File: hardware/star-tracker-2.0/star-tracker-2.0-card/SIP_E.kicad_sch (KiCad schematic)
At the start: 1 part, among them U7 OSD3358-512M-BSM

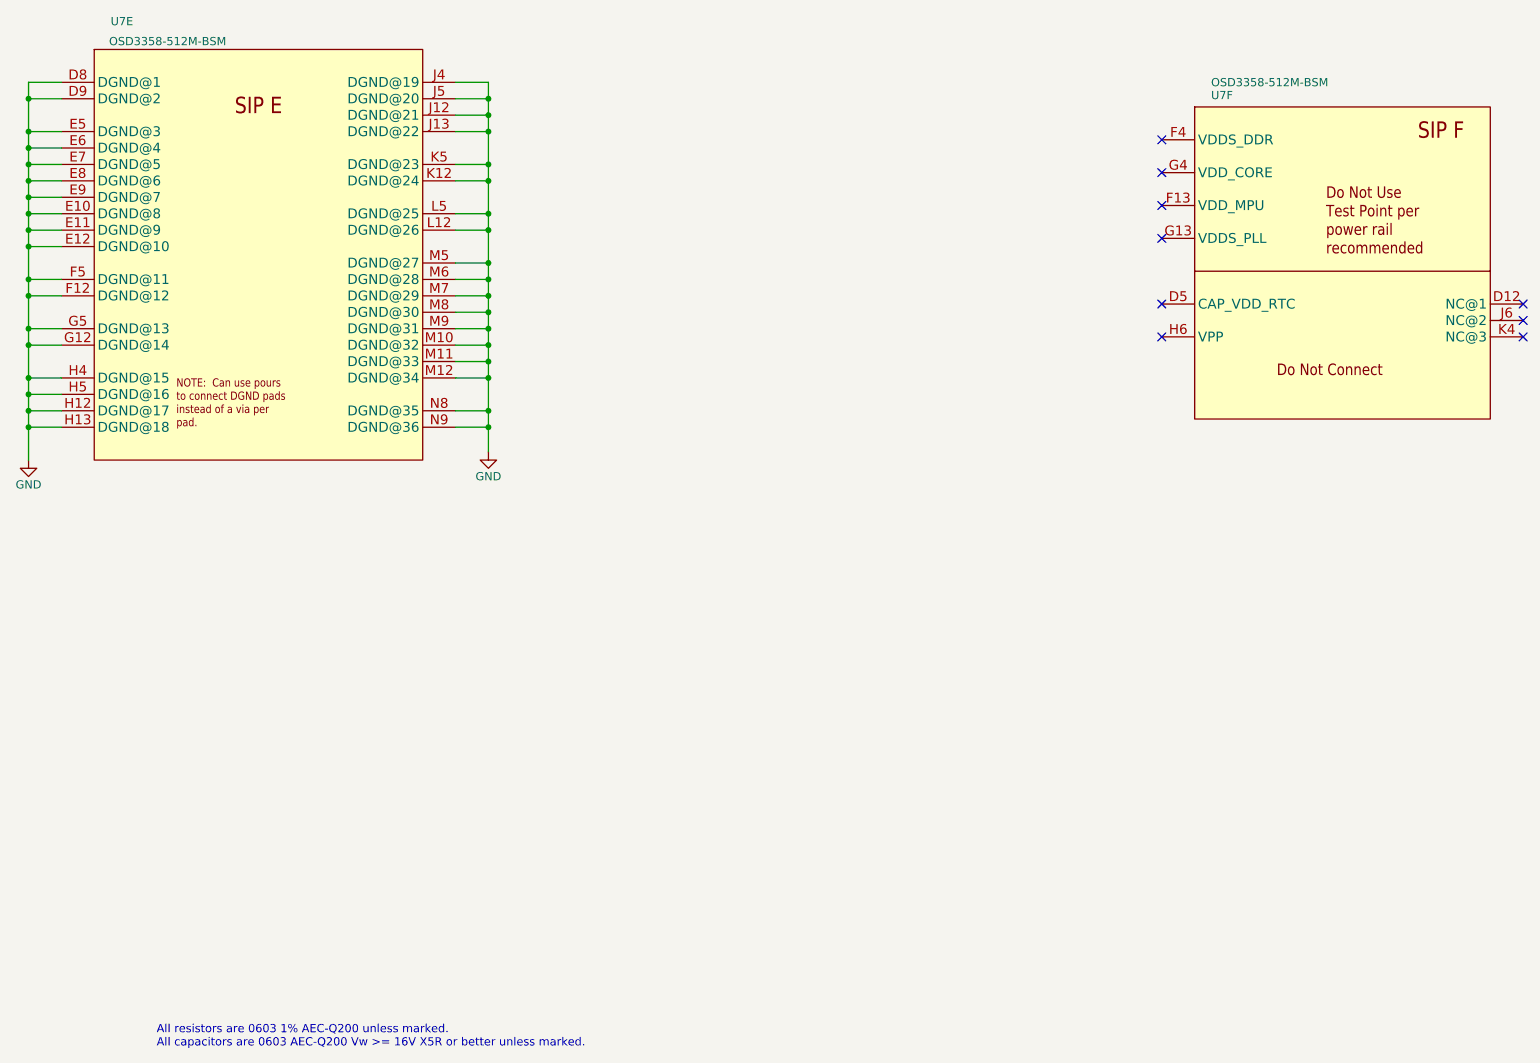
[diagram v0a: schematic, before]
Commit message: Star tracker board update
Added 3d models to footprints, reannotated component designators
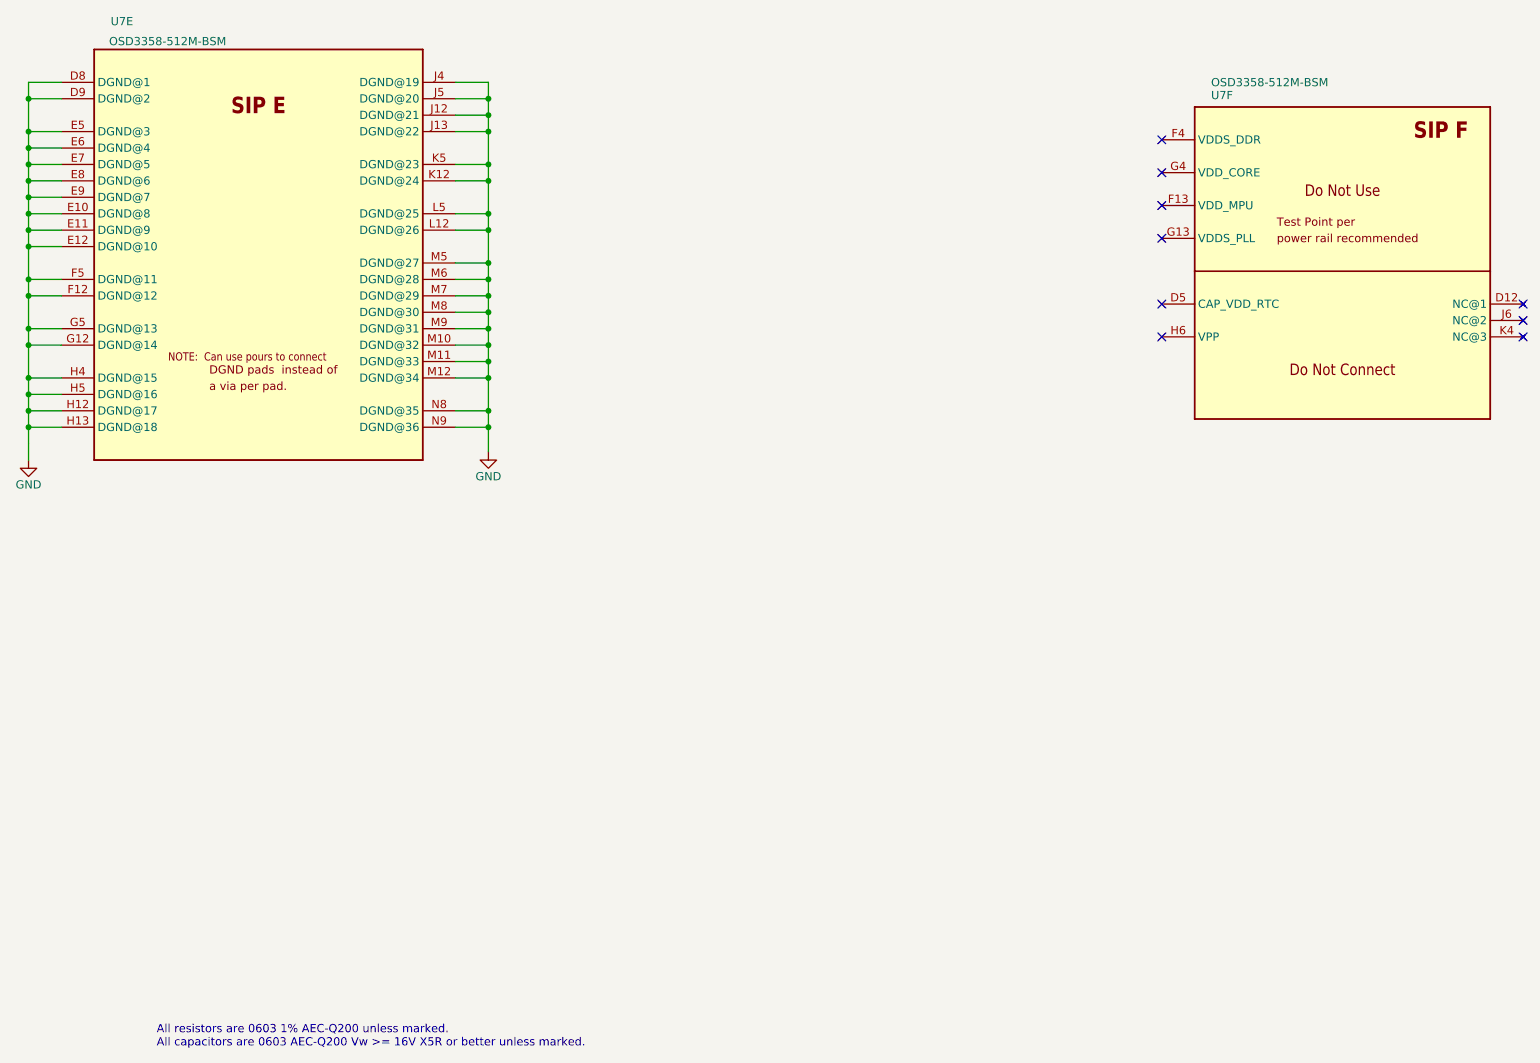
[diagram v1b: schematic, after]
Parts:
- U7: footprint star-tracker-card:OSD335X-BGA-256 -> oresat-ics:U-Octavo-OSD335X-BGA-256; symbol star-tracker-card-eagle-import:OSD3358-512M-BSM -> oresat-ics:OSD3358-512M-BSM; Distributor (none) -> DigiKey; MPN OSD3358-1G-ISM -> OSD3358-512M-BSM
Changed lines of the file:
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@@
 	(title_block
 		(title "OreSat Star Tracker")
-		(date "2026-04-22")
-		(rev "1.3")
+		(date "2026-06-05")
+		(rev "2.0")
 		(company "Portland State Aerospace Society")
 	)
@@
 	)
 	(symbol
-		(lib_id "star-tracker-card-eagle-import:OSD3358-512M-BSM")
+		(lib_id "oresat-ics:OSD3358-512M-BSM")
 		(at 128.27 142.24 0)
 		(unit 5)
@@
 			)
 		)
-		(property "Footprint" "star-tracker-card:OSD335X-BGA-256"
-			(at 128.27 142.24 0)
+		(property "Footprint" "oresat-ics:U-Octavo-OSD335X-BGA-256"
+			(at 128.27 34.29 0)
 			(hide yes)
 			(show_name no)
@@
 			)
 		)
-		(property "Description" "OSD335x Embedded Module ARM® Cortex®-A8, AM3358 1GHz 1GB"
-			(at 128.27 142.24 0)
+		(property "Description" "OSD335x Embedded Module 1GHz 512MB"
+			(at 128.27 38.1 0)
 			(hide yes)
 			(show_name no)
@@
 			)
 		)
-		(property "MPN" "OSD3358-1G-ISM"
-			(at 128.27 142.24 0)
+		(property "MPN" "OSD3358-512M-BSM"
+			(at 128.27 43.18 0)
+			(hide yes)
+			(show_name no)
+			(do_not_autoplace no)
+			(effects
+				(font
+					(size 1.27 1.27)
+				)
+			)
+		)
+		(property "Distributor" "DigiKey"
+			(at 128.27 40.64 0)
 			(hide yes)
 			(show_name no)
@@
 		(in_pos_files yes)
 		(dnp no)
-		(property "Reference" "#PWR74"
+		(property "Reference" "#PWR063"
 			(at 163.83 180.34 0)
 			(hide yes)
@@
 			(project "star-tracker-card"
 				(path "/324e9eb5-7420-4b7e-862c-cc20bb28618a/eb575624-9a53-42ad-b889-70334a877908"
-					(reference "#PWR74")
+					(reference "#PWR063")
 					(unit 1)
 				)
@@
 	)
 	(symbol
-		(lib_id "star-tracker-card-eagle-import:OSD3358-512M-BSM")
+		(lib_id "oresat-ics:OSD3358-512M-BSM")
 		(at 295.91 146.05 0)
 		(unit 6)
@@
 			)
 		)
-		(property "Footprint" "star-tracker-card:OSD335X-BGA-256"
-			(at 295.91 146.05 0)
+		(property "Footprint" "oresat-ics:U-Octavo-OSD335X-BGA-256"
+			(at 295.91 38.1 0)
 			(hide yes)
 			(show_name no)
@@
 			)
 		)
-		(property "Description" "OSD335x Embedded Module ARM® Cortex®-A8, AM3358 1GHz 1GB"
-			(at 295.91 146.05 0)
+		(property "Description" "OSD335x Embedded Module 1GHz 512MB"
+			(at 295.91 41.91 0)
 			(hide yes)
 			(show_name no)
@@
 			)
 		)
-		(property "MPN" "OSD3358-1G-ISM"
-			(at 295.91 146.05 0)
+		(property "MPN" "OSD3358-512M-BSM"
+			(at 295.91 46.99 0)
+			(hide yes)
+			(show_name no)
+			(do_not_autoplace no)
+			(effects
+				(font
+					(size 1.27 1.27)
+				)
+			)
+		)
+		(property "Distributor" "DigiKey"
+			(at 295.91 44.45 0)
 			(hide yes)
 			(show_name no)
@@
 		(in_pos_files yes)
 		(dnp no)
-		(property "Reference" "#PWR73"
+		(property "Reference" "#PWR062"
 			(at 92.71 181.61 0)
 			(hide yes)
@@
 			(project "star-tracker-card"
 				(path "/324e9eb5-7420-4b7e-862c-cc20bb28618a/eb575624-9a53-42ad-b889-70334a877908"
-					(reference "#PWR73")
+					(reference "#PWR062")
 					(unit 1)
 				)
